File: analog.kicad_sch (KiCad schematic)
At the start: 42 parts, among them J10 Conn_01x02, J11 Conn_01x02, J9 Conn_01x03, U2 ADS124S08

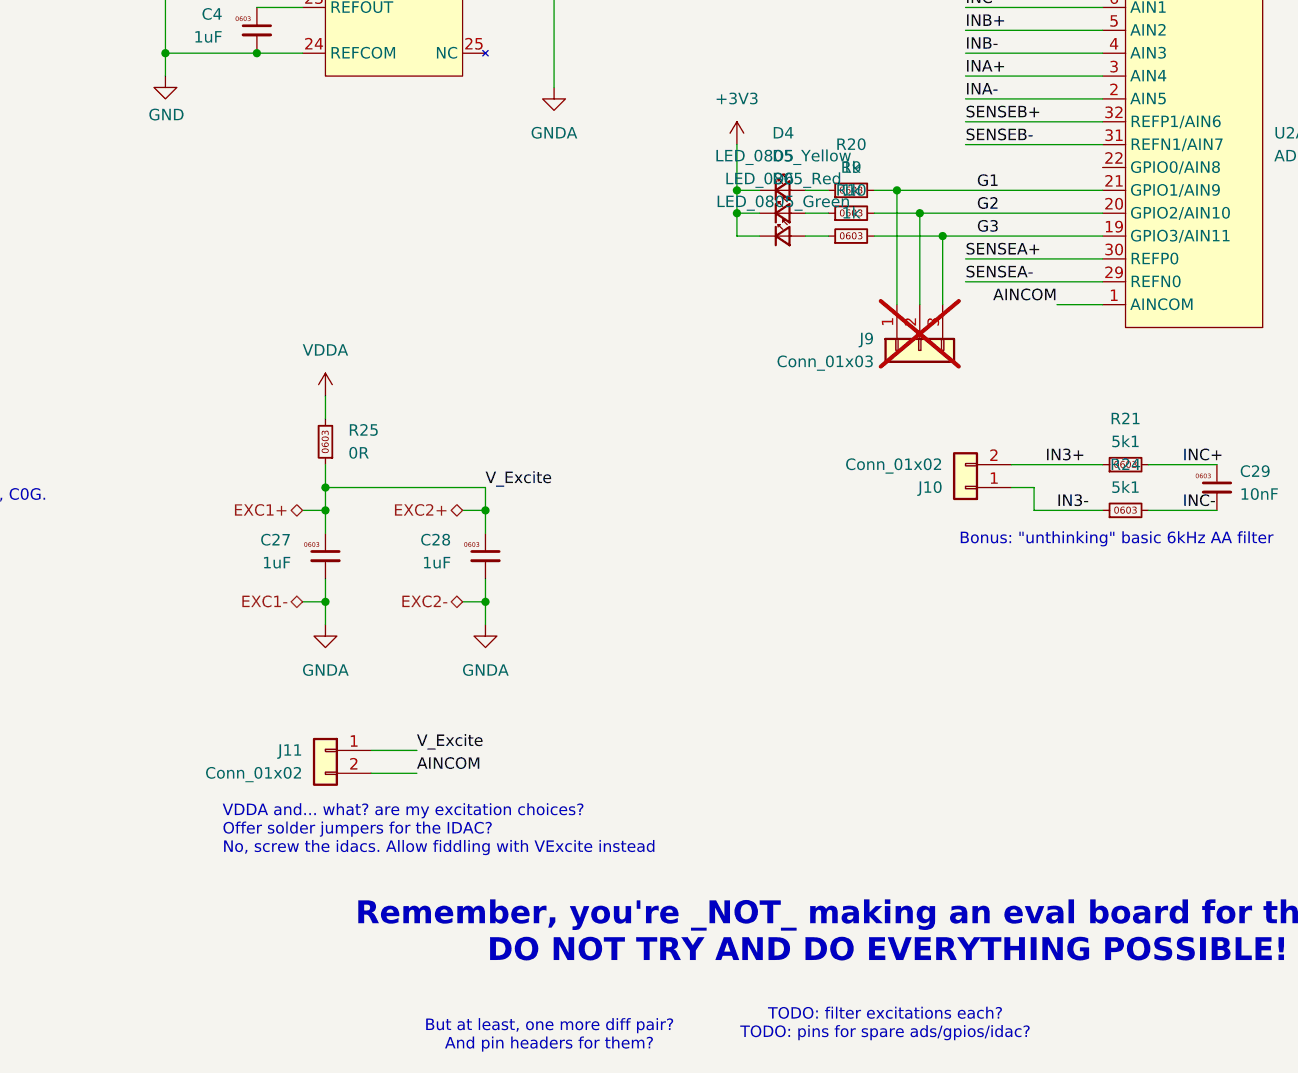
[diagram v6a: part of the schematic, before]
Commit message: "final" to order
added a jumper for aincom to ground.
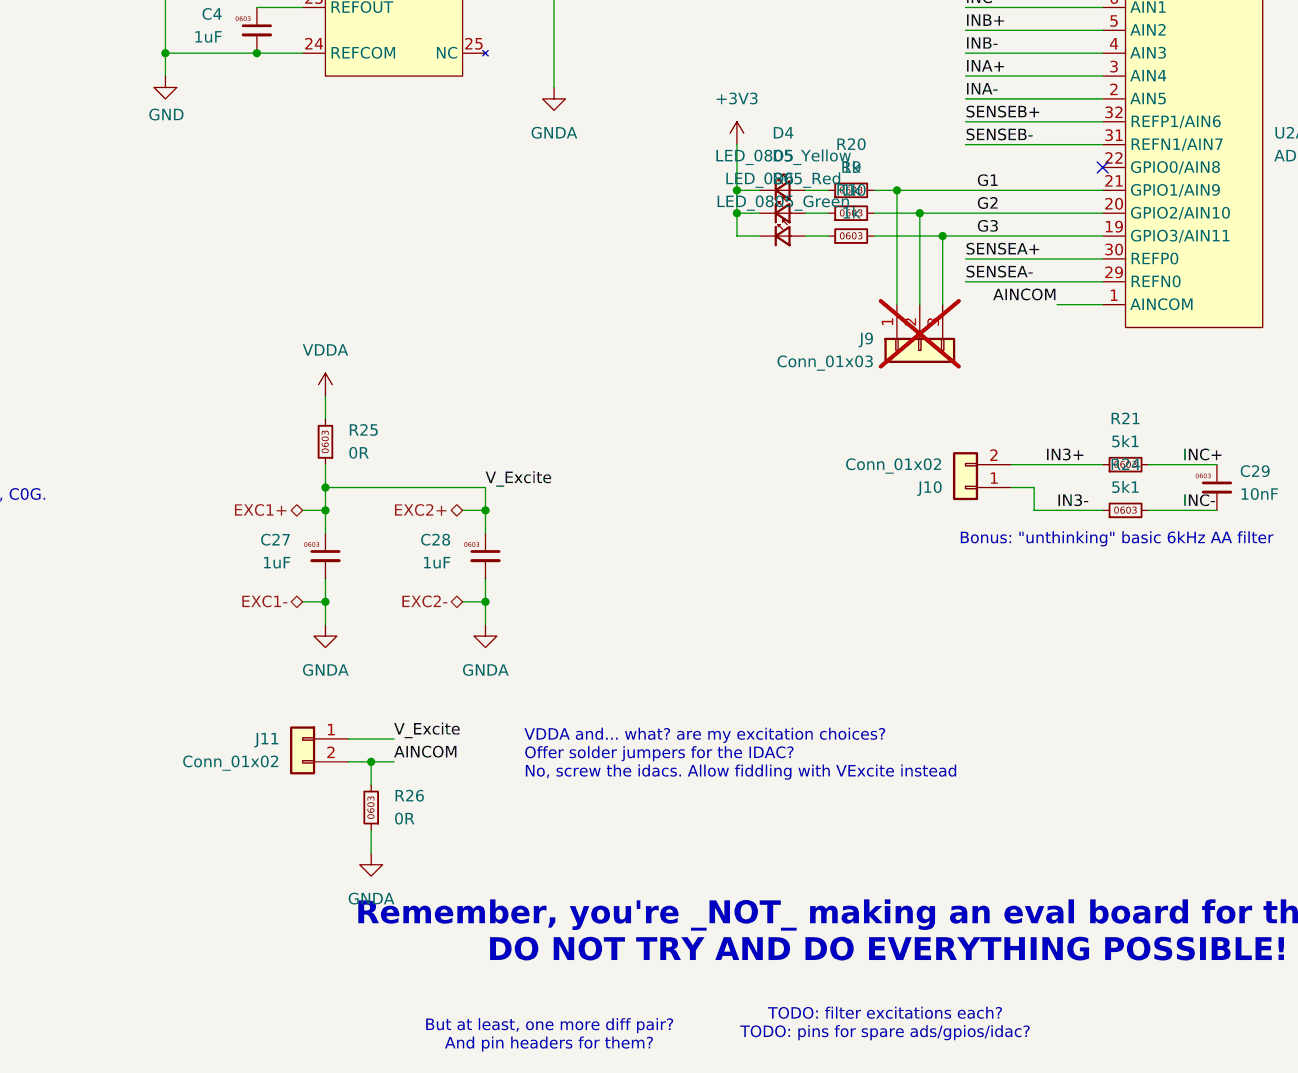
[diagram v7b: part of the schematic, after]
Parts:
- added R26: 0R, Resistor_SMD:R_0603_1608Metric, symbol karl-atomic-basic:KR0603_0R
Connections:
- net AINCOM: now also R26.2
- net GNDA: now also R26.1
- no-connect marks 0 -> 1
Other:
- moved on the sheet: J11
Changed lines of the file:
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@@
 	(text "VDDA and... what? are my excitation choices?\nOffer solder jumpers for the IDAC?\nNo, screw the idacs. Allow fiddling with VExcite instead"
 		(exclude_from_sim no)
-		(at 143.51 137.16 0)
+		(at 177.038 128.778 0)
 		(effects
 			(font
@@
 	)
 	(junction
+		(at 160.02 129.54)
+		(diameter 0)
+		(color 0 0 0 0)
+	)
+	(junction
 		(at 96.52 147.32)
 		(diameter 0)
@@
 		(color 0 0 0 0)
 	)
+	(no_connect
+		(at 241.3 63.5)
+	)
 	(wire
 		(pts
@@
 	(wire
 		(pts
+			(xy 160.02 129.54) (xy 160.02 132.08)
+		)
+		(stroke
+			(width 0)
+			(type default)
+		)
+	)
+	(wire
+		(pts
 			(xy 226.06 43.18) (xy 241.3 43.18)
 		)
@@
 	(wire
 		(pts
-			(xy 160.02 130.81) (xy 165.1 130.81)
+			(xy 157.48 129.54) (xy 160.02 129.54)
 		)
 		(stroke
@@
 	(wire
 		(pts
-			(xy 165.1 128.27) (xy 160.02 128.27)
+			(xy 162.56 127) (xy 157.48 127)
 		)
 		(stroke
@@
 	(wire
 		(pts
+			(xy 160.02 129.54) (xy 162.56 129.54)
+		)
+		(stroke
+			(width 0)
+			(type default)
+		)
+	)
+	(wire
+		(pts
 			(xy 71.12 177.8) (xy 96.52 177.8)
 		)
@@
 	(wire
 		(pts
+			(xy 160.02 137.16) (xy 160.02 139.7)
+		)
+		(stroke
+			(width 0)
+			(type default)
+		)
+	)
+	(wire
+		(pts
 			(xy 71.12 154.94) (xy 71.12 157.48)
 		)
@@
 	)
 	(label "AINCOM"
-		(at 165.1 130.81 0)
+		(at 162.56 129.54 0)
 		(effects
 			(font
@@
 	)
 	(label "V_Excite"
-		(at 165.1 128.27 0)
+		(at 162.56 127 0)
 		(effects
 			(font
@@
 	)
 	(symbol
+		(lib_id "karl-atomic-basic:KR0603_0R")
+		(at 160.02 134.62 180)
+		(unit 1)
+		(exclude_from_sim no)
+		(in_bom yes)
+		(on_board yes)
+		(dnp no)
+		(fields_autoplaced yes)
+		(property "Reference" "R26"
+			(at 162.56 133.3499 0)
+			(effects
+				(font
+					(size 1.27 1.27)
+				)
+				(justify right)
+			)
+		)
+		(property "Value" "0R"
+			(at 162.56 135.8899 0)
+			(effects
+				(font
+					(size 1.27 1.27)
+				)
+				(justify right)
+			)
+		)
+		(property "Footprint" "Resistor_SMD:R_0603_1608Metric"
+			(at 160.02 134.62 0)
+			(effects
+				(font
+					(size 1.27 1.27)
+				)
+				(hide yes)
+			)
+		)
+		(property "Datasheet" "~"
+			(at 160.02 134.62 0)
+			(effects
+				(font
+					(size 1.27 1.27)
+				)
+				(hide yes)
+			)
+		)
+		(property "Description" "Resistor, 0603"
+			(at 160.02 134.62 0)
+			(effects
+				(font
+					(size 1.27 1.27)
+				)
+				(hide yes)
+			)
+		)
+		(property "LCSC Part #" "C21189"
+			(at 160.02 134.62 0)
+			(effects
+				(font
+					(size 1.27 1.27)
+				)
+				(hide yes)
+			)
+		)
+		(property "MPN" "0603WAF0000T5E"
+			(at 160.02 134.62 0)
+			(effects
+				(font
+					(size 1.27 1.27)
+				)
+				(hide yes)
+			)
+		)
+		(property "jlcbasic" "basic"
+			(at 160.02 134.62 0)
+			(effects
+				(font
+					(size 1.27 1.27)
+				)
+				(hide yes)
+			)
+		)
+		(pin "2"
+		)
+		(pin "1"
+		)
+		(instances
+			(project "pi-hat-ads124s08_r1"
+				(path "/e63e39d7-6ac0-4ffd-8aa3-1841a4541b55/c6a2984f-bea9-4fd5-89c5-8bfdade63ac6"
+					(reference "R26")
+					(unit 1)
+				)
+			)
+		)
+	)
+	(symbol
 		(lib_id "karl-atomic-basic:KC0603_100pF")
 		(at 83.82 152.4 0)
@@
 	)
 	(symbol
+		(lib_id "power:GNDA")
+		(at 160.02 139.7 0)
+		(unit 1)
+		(exclude_from_sim no)
+		(in_bom yes)
+		(on_board yes)
+		(dnp no)
+		(fields_autoplaced yes)
+		(property "Reference" "#PWR030"
+			(at 160.02 146.05 0)
+			(effects
+				(font
+					(size 1.27 1.27)
+				)
+				(hide yes)
+			)
+		)
+		(property "Value" "GNDA"
+			(at 160.02 144.78 0)
+			(effects
+				(font
+					(size 1.27 1.27)
+				)
+			)
+		)
+		(property "Footprint" ""
+			(at 160.02 139.7 0)
+			(effects
+				(font
+					(size 1.27 1.27)
+				)
+				(hide yes)
+			)
+		)
+		(property "Datasheet" ""
+			(at 160.02 139.7 0)
+			(effects
+				(font
+					(size 1.27 1.27)
+				)
+				(hide yes)
+			)
+		)
+		(property "Description" "Power symbol creates a global label with name \"GNDA\" , analog ground"
+			(at 160.02 139.7 0)
+			(effects
+				(font
+					(size 1.27 1.27)
+				)
+				(hide yes)
+			)
+		)
+		(pin "1"
+		)
+		(instances
+			(project "pi-hat-ads124s08_r1"
+				(path "/e63e39d7-6ac0-4ffd-8aa3-1841a4541b55/c6a2984f-bea9-4fd5-89c5-8bfdade63ac6"
+					(reference "#PWR030")
+					(unit 1)
+				)
+			)
+		)
+	)
+	(symbol
 		(lib_id "karl-atomic-basic:KC1206_220nF_C0G")
 		(at 96.52 172.72 0)
@@
 	(symbol
 		(lib_id "Connector_Generic:Conn_01x02")
-		(at 154.94 128.27 0)
+		(at 152.4 127 0)
 		(mirror y)
 		(unit 1)
@@
 		(fields_autoplaced yes)
 		(property "Reference" "J11"
-			(at 152.4 128.2699 0)
+			(at 149.86 126.9999 0)
 			(effects
 				(font
@@
 		)
 		(property "Value" "Conn_01x02"
-			(at 152.4 130.8099 0)
+			(at 149.86 129.5399 0)
 			(effects
 				(font
@@
 		)
 		(property "Footprint" "Connector_Phoenix_MC:PhoenixContact_MCV_1,5_2-G-3.81_1x02_P3.81mm_Vertical"
-			(at 154.94 128.27 0)
+			(at 152.4 127 0)
 			(effects
 				(font
@@
 		)
 		(property "Datasheet" "~"
-			(at 154.94 128.27 0)
+			(at 152.4 127 0)
 			(effects
 				(font
@@
 		)
 		(property "Description" "Generic connector, single row, 01x02, script generated (kicad-library-utils/schlib/autogen/connector/)"
-			(at 154.94 128.27 0)
+			(at 152.4 127 0)
 			(effects
 				(font
@@
 		)
 		(property "MPN" "WJ15EDGVC-3.81-2P"
-			(at 154.94 128.27 0)
+			(at 152.4 127 0)
 			(effects
 				(font
@@
 		)
 		(property "LCSC Part #" "C8396"
-			(at 154.94 128.27 0)
+			(at 152.4 127 0)
 			(effects
 				(font
